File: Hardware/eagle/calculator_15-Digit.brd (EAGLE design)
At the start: 154.9 x 53.3 mm, 145 parts, among them IC1 74HC4053P, M1 IRLML6402, M10 IRLML6402, M11 IRLML6402, M12 IRLML6402, M2 IRLML6402, M3 IRLML6402, M4 IRLML6402, M5 IRLML6402, M6 IRLML6402, M7 IRLML6402, M8 IRLML6402, M9 IRLML6402, U1 74HC4051_MUXDIL_16, U2 TC1262-3.3VDB, U3 ATMEGA1284P-PU, U5 CON, X1 MICROMATCH-12, X2 MICROMATCH-12, X3 MICROMATCH-12, X4 MICROMATCH-12, Y2 12MHz

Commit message: Switch-block changed Rev.02
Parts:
- removed BAT1, BAT2, BAT3: NimH_AAA, SparkFun-Electromechanical:BATTERY-AAA-KIT
- added BH1, BH2, BH3: BATTERY_HOLDER_AAAHOLDER_AAA, SparkFun-Electromechanical:BATTERY-AAA-KIT
- added U$4, U$5: HOLDER_AAA_LEFT1, SparkFun-Electromechanical:BATTERY-AAA-LEFT
- added U$6: HOLDER_AAA_RIGHT, SparkFun-Electromechanical:BATTERY-AAA-RIGHT
- D14, D15, D16, D17, D18, D19, D2, D20, D21, D22, D23, D24, D25, D26, D27: value SC40-11_UNI -> SC40-11_UNISC40-11_UNI
- R10, R11, R12, R13, R14, R15, R16, R17, R18, R19, R5, R6, R7, R8, R9: device rcl:0204/7 -> rcl:R1210
- moved U1 52.1 mm to (77.5, -21.6)
- moved M11 7.73 mm to (123.2, 19.1)
- moved M9 7.73 mm to (120.0, 19.1)
- moved M10 7.73 mm to (121.9, 19.1)
- moved M8 7.73 mm to (118.7, 19.1)
- moved JP9 3.09 mm to (43.3, 31.9)
- moved JP12 3.06 mm to (139.4, 31.9)
- moved JP7 3.06 mm to (136.9, 31.9)
- moved JP11 2.84 mm to (134.4, 31.9)
- moved X3 2.27 mm to (123.2, 31.5)
- moved X1 2.27 mm to (31.8, 31.5)
- moved JP10 2.09 mm to (45.8, 31.9)
- moved JP8 2.09 mm to (48.4, 31.9)
- moved X4 1.63 mm to (123.2, 14.7)
- moved X2 1.63 mm to (31.8, 14.7)
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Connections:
- new net NC1: U$4.P1, U$4.P2
- new net NC2: U$5.P1, U$5.P2
- new net NC3: U$6.M1, U$6.M2
- net DIG_0: now also D2.23, D2.28
- net DIG_1: now also D14.23, D14.28
- net DIG_10: now also D23.23, D23.28
- net DIG_11: now also D24.23, D24.28
- net DIG_12: now also D25.23, D25.28
- net DIG_13: now also D26.23, D26.28
- net DIG_14: now also D27.23, D27.28
- net DIG_2: now also D15.23, D15.28
- net DIG_3: now also D16.23, D16.28
- net DIG_4: now also D17.23, D17.28
- net DIG_5: now also D18.23, D18.28
- net DIG_6: now also D19.23, D19.28
- net DIG_7: now also D20.23, D20.28
- net DIG_8: now also D21.23, D21.28
- net DIG_9: now also D22.12, D22.14, D22.23, D22.28
- net GND: now also BH1.M1, BH1.M2; no longer BAT3.GND@1
- net N$2: now also BH1.P1, BH1.P2, BH2.M1, BH2.M2; no longer BAT2.GND@1, BAT3.PWR@1
- net N$3: now also BH2.P1, BH2.P2, BH3.M1, BH3.M2; no longer BAT1.GND@1, BAT2.PWR@1
- net SEG_A: now also D14.27, D15.27, D16.27, D17.27, D18.27, D19.27, D2.27, D20.27, D21.27, D22.27, D23.27, D24.27, D25.27, D26.27, D27.27
- net SEG_B: now also D14.26, D15.26, D16.26, D17.26, D18.26, D19.26, D2.26, D20.26, D21.26, D22.26, D23.26, D24.26, D25.26, D26.26, D27.26
- net SEG_C: now also D14.24, D15.24, D16.24, D17.24, D18.24, D19.24, D2.24, D20.24, D21.24, D22.24, D23.24, D24.24, D25.24, D26.24, D27.24
- net SEG_D: now also D14.22, D15.22, D16.22, D17.22, D18.22, D19.22, D2.22, D20.22, D21.22, D22.22, D23.22, D24.22, D25.22, D26.22, D27.22
- net SEG_DP: now also D14.25, D15.25, D16.25, D17.25, D18.25, D19.25, D2.25, D20.25, D21.25, D22.25, D23.25, D24.25, D25.25, D26.25, D27.25
- net SEG_E: now also D14.21, D15.21, D16.21, D17.21, D18.21, D19.21, D2.21, D20.21, D21.21, D22.21, D23.21, D24.21, D25.21, D26.21, D27.21
- net SEG_F: now also D14.29, D15.29, D16.29, D17.29, D18.29, D19.29, D2.29, D20.29, D21.29, D22.29, D23.29, D24.29, D25.29, D26.29, D27.29
- net SEG_G: now also D14.30, D15.30, D16.30, D17.30, D18.30, D19.30, D2.30, D20.30, D21.30, D22.30, D23.30, D24.30, D25.30, D26.30, D27.30
- net VCC: now also BH3.P1, BH3.P2; no longer BAT1.PWR@1
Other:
- outline, holes or cut-outs redrawn

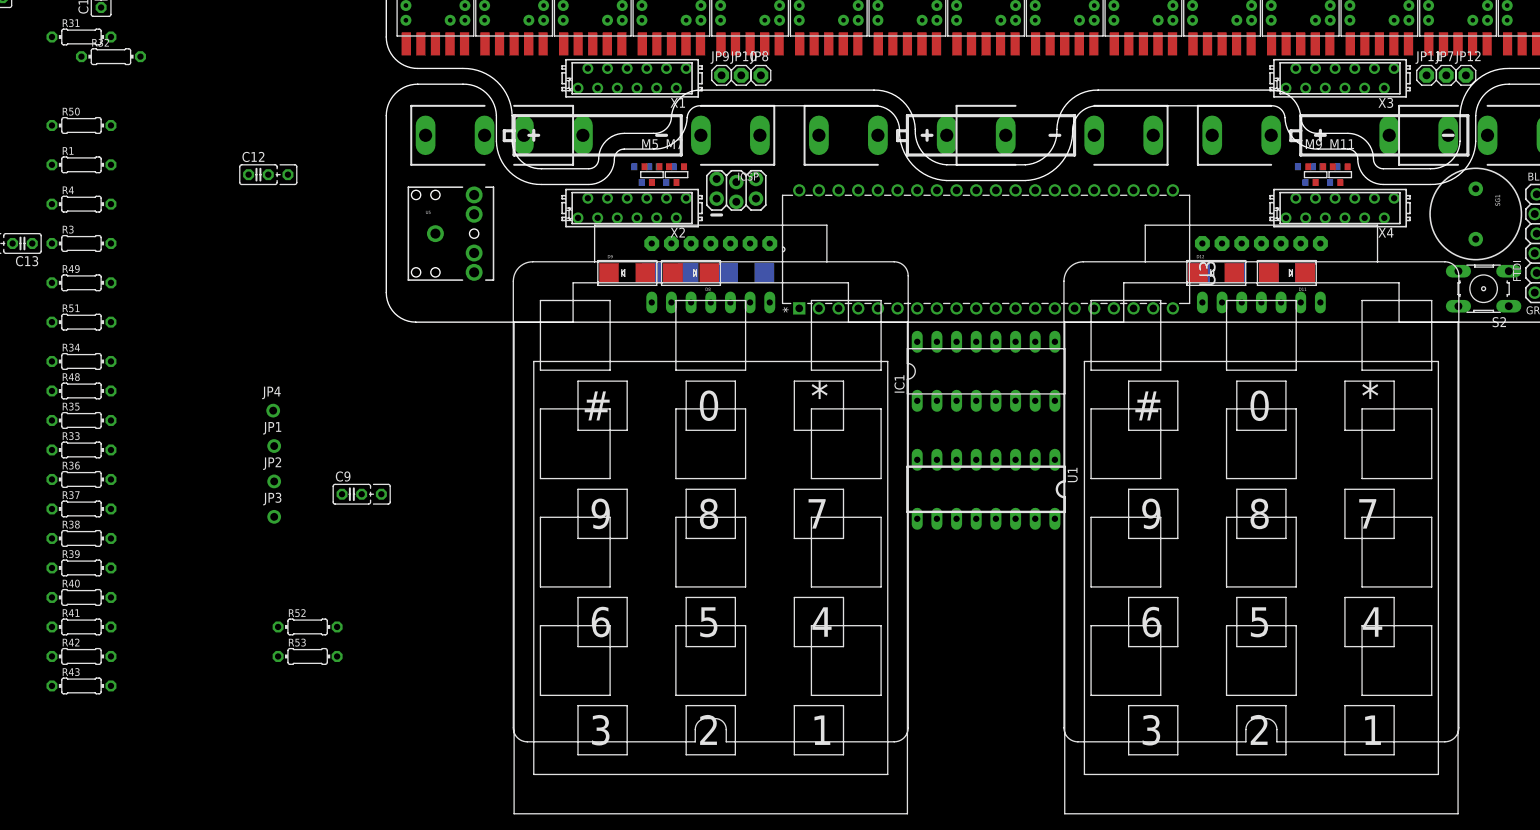
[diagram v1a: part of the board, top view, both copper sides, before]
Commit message: Switch-block Filter added
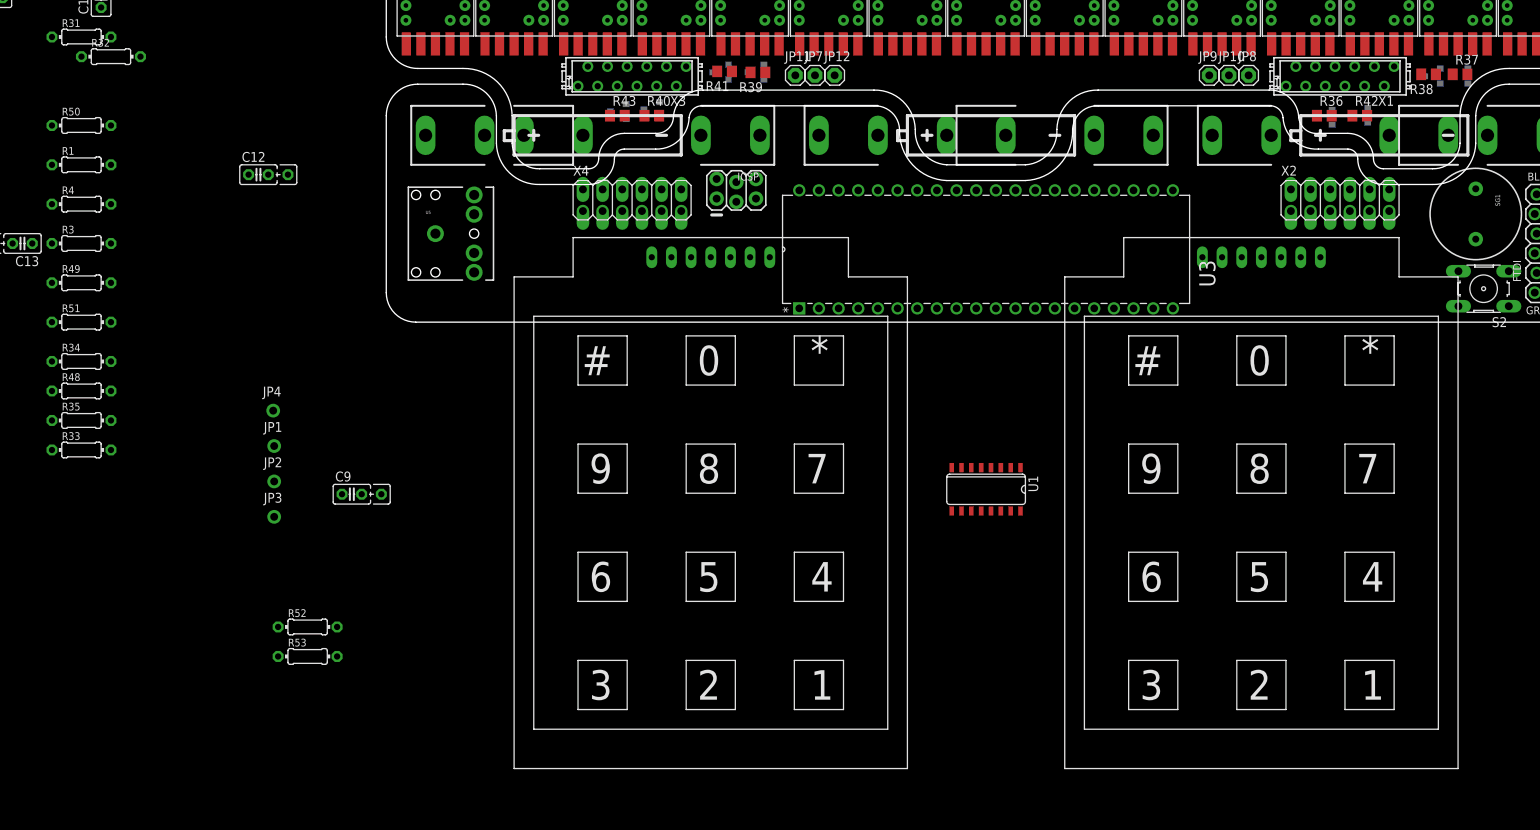
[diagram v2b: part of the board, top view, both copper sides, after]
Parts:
- removed D10, D11, D12, D13, D6, D7, D8, D9: SD103CW, BaseApp:SMADIODE
- removed IC1: 74HC4053P, 74xx-eu:DIL16
- removed U$1, U$3: KEYBOARD, &my:KEYBOARD
- R36, R37, R38, R39, R40, R41, R42, R43: device rcl:0204/7 -> rcl:R0805
- U1: value 74HC4051_MUXDIL_16 -> 74HC4051_MUX; device SparkFun-AnalogIC:DIL16 -> SparkFun-AnalogIC:SO16
- X2, X4: value MICROMATCH-12 -> (none); device Con-amp-micromatch:MICROMATCH-12 -> pinhead:2X06
- moved R37 186.7 mm to (138.7, 32.0)
- moved R38 184.0 mm to (134.6, 32.0), turned to 180 degrees
- moved R42 179.3 mm to (125.7, 26.7)
- moved R36 167.3 mm to (121.2, 26.7)
- moved R41 109.8 mm to (43.7, 32.4), turned to 180 degrees
- moved R39 108.3 mm to (48.0, 32.3), turned to 180 degrees
- moved M5 105.2 mm to (138.7, 31.8), flipped to the bottom, turned to 90 degrees
- moved R43 101.1 mm to (29.8, 26.7)
- moved M7 98.5 mm to (135.1, 31.8), flipped to the bottom, turned to 90 degrees
- moved R40 96.4 mm to (34.3, 26.7)
- moved X2 91.4 mm to (123.2, 15.7), turned to 0 degrees
- moved X4 91.4 mm to (31.8, 15.7), turned to 0 degrees
- moved X1 91.4 mm to (123.2, 31.8)
- moved X3 91.4 mm to (31.8, 31.8)
- moved M6 89.9 mm to (125.7, 26.7), turned to 90 degrees
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- renumbered U$4 to BH4, U$5 to BH5, U$6 to BH6
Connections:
- removed net A0-A: IC1.12, KP2.C_2, U$3.5
- removed net A0-B: IC1.13, KP1.C_2, U$1.5
- removed net A1-A: IC1.2, KP2.C_1, U$3.1
- removed net A1-B: IC1.1, KP1.C_1, U$1.1
- removed net A2-A: IC1.5, KP2.C_0, U$3.3
- removed net A2-B: IC1.3, KP1.C_0, U$1.3
- removed net IO_0: D10.C, M4.1, R36.2, U1.13
- removed net IO_1: D11.C, M5.1, R37.2, U1.14
- removed net IO_2: D12.C, M6.1, R42.2, U1.12
- removed net IO_3: D13.C, M7.1, R38.2, U1.15
- removed net IO_4: D6.C, M8.1, R43.2, U1.2
- removed net IO_5: D7.C, M9.1, R39.2, U1.4
- removed net IO_6: D8.C, M10.1, R40.2, U1.5
- removed net IO_7: D9.C, M11.1, R41.2, U1.1
- removed net IO_S_0: D10.A, KP2.R_0, U$3.2
- removed net IO_S_1: D11.A, KP2.R_1, U$3.7
- removed net IO_S_2: D12.A, KP2.R_2, U$3.6
- removed net IO_S_3: D13.A, KP2.R_3, U$3.4
- removed net IO_S_4: D6.A, KP1.R_0, U$1.2
- removed net IO_S_5: D7.A, KP1.R_1, U$1.7
- removed net IO_S_6: D8.A, KP1.R_2, U$1.6
- removed net IO_S_7: D9.A, KP1.R_3, U$1.4
- removed net N$33: M10.2, M11.2, M3.3, M4.2, M5.2, M6.2, M7.2, M8.2, M9.2, R33.1, R36.1, R37.1, R38.1, R39.1, R40.1, R41.1, R42.1, R43.1
- removed net NC_1: X3.8
- removed net NC_2: X4.8
- removed net SEG-A: M4.3, X2.9
- removed net SEG-B: M5.3, X2.10
- removed net SEG-C: M6.3, X2.11
- removed net SEG-D: M7.3, X2.12
- removed net SEG-DP: M11.3, X4.12
- removed net SEG-E: M8.3, X4.9
- removed net SEG-F: M9.3, X4.10
- removed net SEG-G: M10.3, X4.11
- new net CA_LED: M10.2, M11.2, M4.2, M5.2, M6.2, M7.2, M8.2, M9.2, R36.1, R37.1, R38.1, R39.1, R40.1, R41.1, R42.1, R43.1, X3.8
- new net CA_PWM: M3.3, R33.1, X4.8
- new net IO-A: M4.1, R36.2, X1.9
- new net IO-B: M5.1, R37.2, X1.10
- new net IO-C: M6.1, R42.2, X1.11
- new net IO-D: M7.1, R38.2, X1.12
- new net IO-DP: M11.1, R41.2, X3.12
- new net IO-E: M8.1, R43.2, X3.9
- new net IO-F: M9.1, R39.2, X3.10
- new net IO-G: M10.1, R40.2, X3.11
- new net IO_A: KP2.R_0, U1.13, X2.9
- new net IO_B: KP2.R_1, U1.14, X2.10
- new net IO_C: KP2.R_2, U1.12, X2.11
- new net IO_D: KP2.R_3, U1.15, X2.12
- new net IO_DP: KP1.R_3, U1.1, X4.12
- new net IO_E: KP1.R_0, U1.2, X4.9
- new net IO_F: KP1.R_1, U1.4, X4.10
- new net IO_G: KP1.R_2, U1.5, X4.11
- net A1: no longer IC1.10, IC1.11, IC1.9
- net A_0: now also KP1.C_2, KP2.C_2; no longer IC1.14
- net A_1: now also KP1.C_1, KP2.C_1; no longer IC1.15
- net A_2: now also KP1.C_0, KP2.C_0; no longer IC1.4
- net GND: no longer IC1.7, IC1.8
- net INH: no longer IC1.6
- net SEG_A: now also M4.3; no longer X1.9
- net SEG_B: now also M5.3; no longer X1.10
- net SEG_C_SOURCE: now also M6.3; no longer X1.11
- net SEG_D: now also M7.3; no longer X1.12
- net SEG_DP_SOURCE: now also M11.3; no longer X3.12
- net SEG_E: now also M8.3; no longer X3.9
- net SEG_F: now also M9.3; no longer X3.10
- net SEG_G: now also M10.3; no longer X3.11
- net V_IN: no longer IC1.16
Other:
- outline, holes or cut-outs redrawn
- board text added: "CERN OHL v.1.2 or later"
- board text added: "http://ohwr.org/cernohl"
- board text added: "https://oshpark.com/profiles/Jens_G"
- board text added: "snc98 - Slash Number Calculator Rev. 0.8"
- board text removed: "CC BY-SA"
- board text removed: "Calculator 15-Digit with 1284P"
- board text removed: "goo.gl/5fAHca"
- board text removed: "jg 0915 Rev.0.6"

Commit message: New Picture "Switch mechanical"
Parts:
- moved KP1 1.27 mm to (40.6, 8.38)
- moved KP2 1.27 mm to (114.3, 8.38)
- moved U3 1.27 mm to (100.3, 17.0)

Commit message: Debuglevel 13 - Protokoll Statepoint
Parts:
- added R29, R30, R54, R55, R56, R57, R58, R59: 3k3, rcl:0204/5
- R36, R37, R38, R39, R40, R41, R42, R43: device rcl:R0805 -> rcl:R1206
- moved C8 175.8 mm to (156.9, -56.8), turned to 180 degrees
- moved C7 174.2 mm to (152.7, -55.3), turned to 0 degrees
- moved LOGO1 168.4 mm to (155.2, -51.5), turned to 270 degrees
- moved C1 163.9 mm to (150.9, -47.8), turned to 180 degrees
- moved Y2 151.8 mm to (155.3, -39.6), turned to 180 degrees
- moved C3 150.1 mm to (146.1, -37.0), turned to 270 degrees
- moved C2 147.7 mm to (163.5, -37.3), turned to 270 degrees
- moved C5 134.8 mm to (152.7, -27.2), turned to 180 degrees
- moved M1 133.6 mm to (157.4, -26.9), turned to 90 degrees
- moved LOGO2 131.2 mm to (152.5, -24.6), turned to 90 degrees
- moved C6 125.1 mm to (156.7, -20.8), turned to 0 degrees
- moved U2 107.9 mm to (163.7, -9.14), turned to 180 degrees
- moved S1 106.5 mm to (155.0, -7.34), turned to 270 degrees
- moved JP4 105.6 mm to (78.5, -61.2), turned to 180 degrees
- moved JP1 101.3 mm to (78.4, -56.6), turned to 180 degrees
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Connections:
- removed net D15_A: R6.2, X1.2
- removed net D19_A: R19.2, X3.7
- removed net D20_A: R18.2, X3.6
- removed net D21_A: R17.2, X3.5
- removed net D22_A: R16.2, X3.4
- removed net D23_A: R15.2, X3.3
- new net D0_A: R5.2, X3.1
- new net D1_A: R6.2, X3.2
- new net D2_A: R7.2, X3.3
- new net D3_A: R8.2, X3.4
- new net D4_A: R9.2, X3.5
- new net D7_A: R12.2, X1.5
- new net IO_A__: X2.9
- new net IO_B__: X2.10
- new net IO_C__: X2.11
- new net IO_D__: X2.12
- net CA_LED: now also R29.1, R30.1, R54.1, R55.1, R56.1, R57.1, R58.1, R59.1
- net D10_A: now also R15.2, X1.8; no longer R11.2, X1.7
- net D11_A: now also R16.2, X1.9; no longer R12.2, X1.8
- net D12_A: now also R17.2, X1.10; no longer R13.2, X3.1
- net D13_A: now also R18.2, X1.11; no longer R14.2, X3.2
- net D14: no longer X2.1
- net D14_A: now also R19.2, X1.12; no longer R5.2, X1.1
- net D15: no longer X2.2
- net D5_A: now also X3.6; no longer X1.6
- net D6_A: now also R11.2, X3.7; no longer R9.2, X1.5
- net D8: no longer X2.3
- net D8_A: now also R13.2, X1.6; no longer R7.2, X1.3
- net D9: no longer X2.4
- net D9_A: now also R14.2, X1.7; no longer R8.2, X1.4
- net IO-A: now also R29.2, X1.4; no longer X1.9
- net IO-B: now also R30.2, X1.3; no longer X1.10
- net IO-C: now also R54.2, X1.2; no longer X1.11
- net IO-D: now also R55.2, X1.1; no longer X1.12
- net IO-DP: now also R59.2, X3.9; no longer X3.12
- net IO-E: now also R56.2, X3.12; no longer X3.9
- net IO-F: now also R57.2, X3.11; no longer X3.10
- net IO-G: now also R58.2, X3.10; no longer X3.11
- net IO_A: now also X2.4; no longer X2.9
- net IO_B: now also X2.3; no longer X2.10
- net IO_C: now also X2.2; no longer X2.11
- net IO_D: now also X2.1; no longer X2.12
- net IO_DP: now also X4.9; no longer X4.12
- net IO_E: now also X4.12; no longer X4.9
- net IO_F: now also X4.11; no longer X4.10
- net IO_G: now also X4.10; no longer X4.11
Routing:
- net SEG_G: track 0.00 -> 337.5 mm
- net SEG_A: track 0.00 -> 335.2 mm
- net SEG_DP: track 0.00 -> 327.7 mm
- net SEG_F: track 0.00 -> 306.0 mm, vias 0 -> 32
- net SEG_C: track 0.00 -> 271.7 mm, vias 0 -> 29
- net SEG_B: track 0.00 -> 267.0 mm, vias 0 -> 15
- net SEG_E: track 0.00 -> 254.6 mm, vias 0 -> 1
- net SEG_D: track 0.00 -> 209.0 mm, vias 0 -> 16
- net CA_LED: track 0.00 -> 163.1 mm, vias 0 -> 4
- net D7_A: track 0.00 -> 65.3 mm, vias 0 -> 1
- net D8_A: track 0.00 -> 52.1 mm
- net D6_A: track 0.00 -> 51.3 mm, vias 0 -> 1
- net IO-A: track 0.00 -> 42.7 mm, vias 0 -> 3
- net D5_A: track 0.00 -> 42.0 mm
- net IO-DP: track 0.00 -> 41.2 mm, vias 0 -> 1
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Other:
- outline, holes or cut-outs redrawn

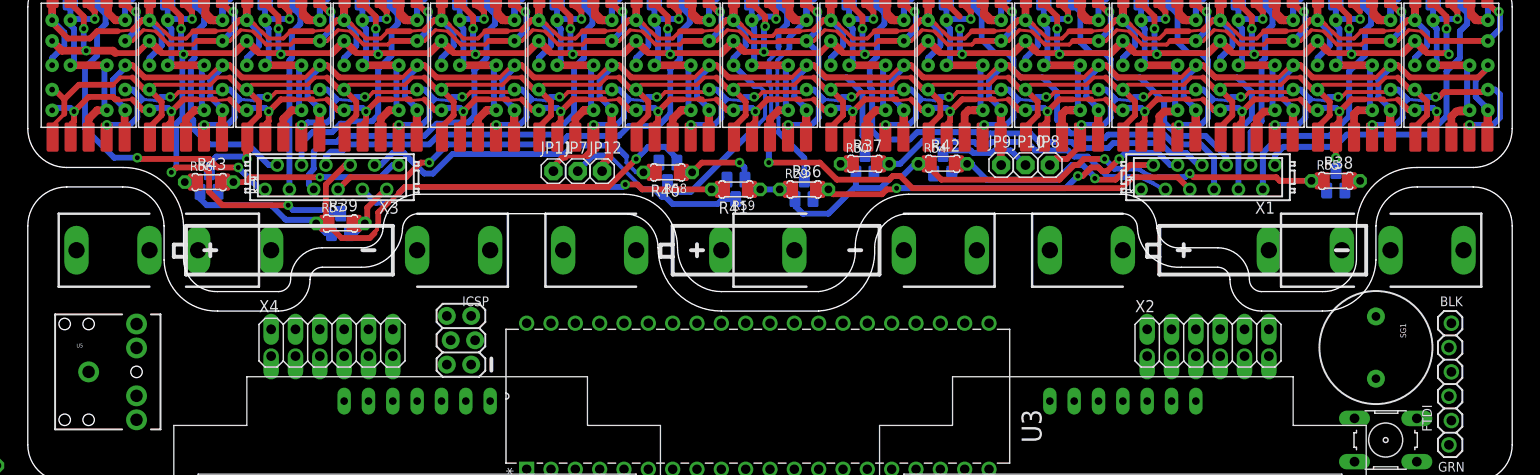
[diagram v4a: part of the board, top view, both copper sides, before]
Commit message: snc98_Display_15x7-Segment_LED_v2
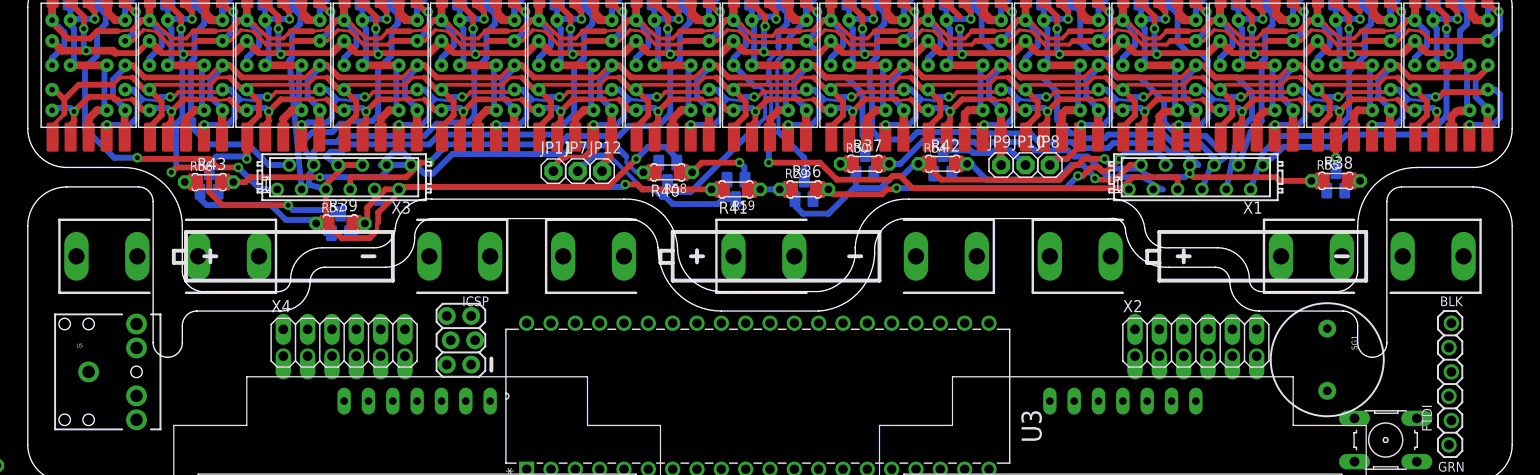
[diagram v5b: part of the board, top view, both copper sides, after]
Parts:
- R21, R22: value 8k2 -> 6k8
- moved SG1 5.24 mm to (135.6, 12.7)
- moved X3 1.27 mm to (33.0, 31.8)
- moved X4 1.27 mm to (33.0, 14.5)
- moved X1 1.27 mm to (121.9, 31.8)
- moved X2 1.27 mm to (121.9, 14.5)
- moved BH1 0.63 mm to (128.3, 23.5)
- moved BH2 0.63 mm to (77.5, 23.5)
- moved BH3 0.63 mm to (26.7, 23.5)
- moved BH4 0.63 mm to (133.3, 23.5)
- moved BH5 0.63 mm to (76.2, 23.5)
- moved BH6 0.63 mm to (21.6, 23.5)
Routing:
- net IO-E: track 21.5 -> 22.7 mm
- net D0_A: track 36.4 -> 37.7 mm
- net IO-F: track 7.87 -> 9.14 mm
- net IO-C: track 25.4 -> 24.1 mm
- net D1_A: track 25.2 -> 26.4 mm
- net CA_LED: track 163.1 -> 164.4 mm
- net D4_A: track 36.3 -> 37.5 mm
- net IO-B: track 35.4 -> 36.2 mm
- net D5_A: track 42.0 -> 42.6 mm
- net D10_A: track 28.3 -> 28.9 mm
- net D14_A: track 34.3 -> 34.9 mm
- net IO-DP: track 41.2 -> 40.6 mm
- net D7_A: track 65.3 -> 64.7 mm
- net D6_A: track 51.3 -> 50.8 mm
- net D8_A: track 52.1 -> 52.6 mm
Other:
- outline, holes or cut-outs redrawn
